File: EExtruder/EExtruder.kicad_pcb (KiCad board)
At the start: 2 copper layers, 66.2 x 47.1 mm, 86 parts, among them J1 20A 50V, J11 Conn_01x03_Male, J2 AudioJack4_Ground, J3 6A 50V, J4 6A 50V, J5 Conn_01x02, J6 Conn_01x02, J7 Conn_01x03_Male, J8 Conn_01x03_Male, J9 Conn_01x03_Male, Q1 DTC124E, Q2 PSMN7R0-30YL, Q3 DTC124E, Q4 PSMN7R0-30YL, Q5 SI2318CDS, Q6 SI2318CDS, Q7 SI2318CDS, U1 STM32F030C8Tx, U2 DCBuck, Y1 8MHz

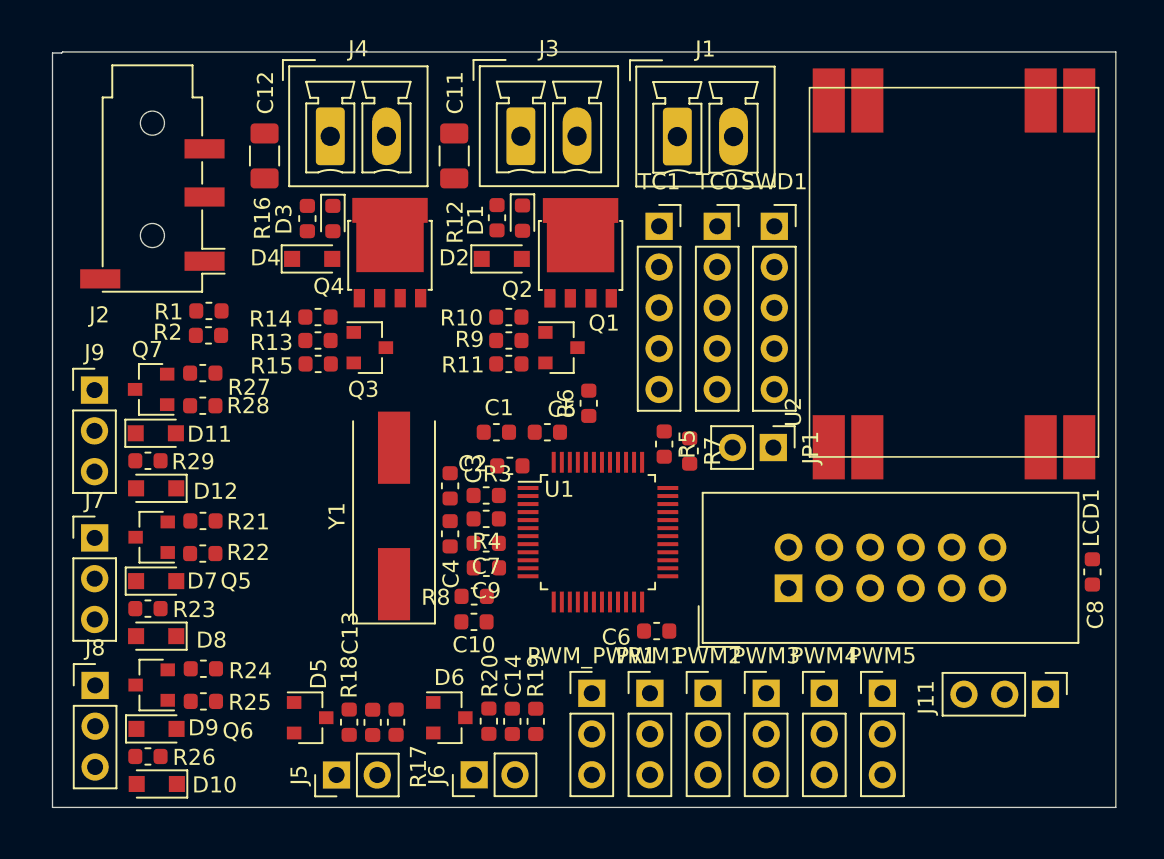
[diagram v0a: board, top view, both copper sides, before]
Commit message: 32 traces to go.
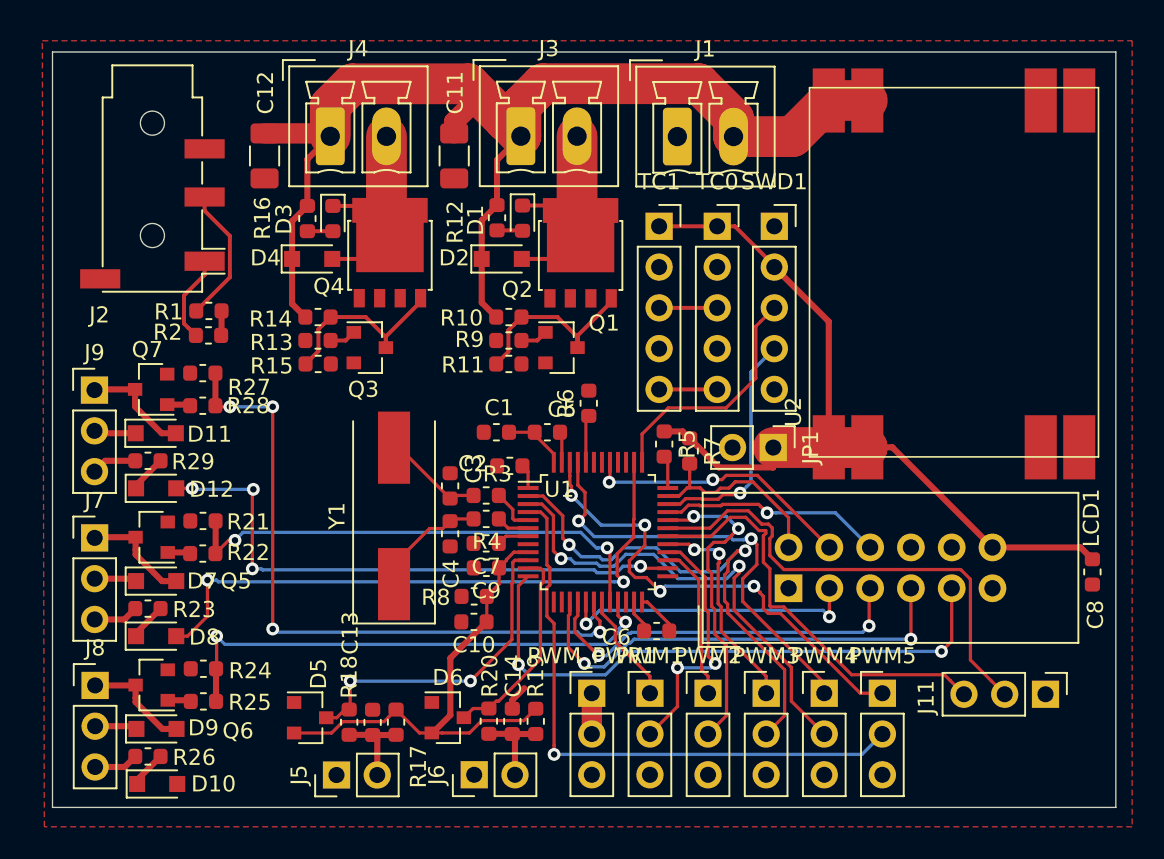
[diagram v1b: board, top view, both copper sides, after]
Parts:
- moved D6 0.10 mm to (152.6, 124.6)
- turned D10 to 0 degrees
- turned D12 to 0 degrees
- turned D8 to 0 degrees
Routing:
- net /VIN: track 0.00 -> 86.0 mm
- net /3.3V: track 0.00 -> 62.4 mm
- net /PWM0: track 0.00 -> 42.1 mm, vias 0 -> 4
- net /TACH_E0: track 0.00 -> 38.7 mm, vias 0 -> 2
- net /TACH5: track 0.00 -> 37.3 mm, vias 0 -> 1
- net /TEMP_EX: track 0.00 -> 37.2 mm, vias 0 -> 2
- net /TACH0: track 0.00 -> 36.0 mm, vias 0 -> 4
- net /SPI_CLK: track 0.00 -> 32.2 mm, vias 0 -> 2
- net /E1_FAN: track 0.00 -> 31.9 mm, vias 0 -> 2
- net /TACH3: track 0.00 -> 31.8 mm, vias 0 -> 2
- net /AVREF: track 0.00 -> 31.2 mm
- net /E0_FAN: track 0.00 -> 30.8 mm, vias 0 -> 2
- net /PWM5: track 0.00 -> 30.4 mm, vias 0 -> 4
- net /UART_RX: track 0.00 -> 30.3 mm
- net /TACH4: track 0.00 -> 30.2 mm, vias 0 -> 2
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- added copper zone on F.Cu, net GND
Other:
- outline, holes or cut-outs redrawn

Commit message: Unrouted - only power.
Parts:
- moved JP1 28.8 mm to (144.1, 106.6), turned to 0 degrees
- moved C10 6.51 mm to (148.6, 122.0)
- moved C9 5.82 mm to (156.5, 120.9), turned to 90 degrees
- moved R8 5.48 mm to (158.1, 120.9), turned to 90 degrees
- moved R7 5.00 mm to (172.6, 108.6)
- moved R5 4.95 mm to (170.9, 108.6)
- moved C7 1.07 mm to (154.2, 114.5), turned to 270 degrees
- moved R6 0.96 mm to (162.3, 104.7), turned to 0 degrees
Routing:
- net /3.3V: track 62.4 -> 9.73 mm
- net /PWM0: track 42.1 -> 2.03 mm, vias 4 -> 0
- net /TACH_E0: track 38.7 -> 0.00 mm, vias 2 -> 0
- net /TACH5: track 37.3 -> 0.00 mm, vias 1 -> 0
- net /TEMP_EX: track 37.2 -> 0.00 mm, vias 2 -> 0
- net /TACH0: track 36.0 -> 0.00 mm, vias 4 -> 0
- net /SPI_CLK: track 32.2 -> 0.00 mm, vias 2 -> 0
- net /TACH3: track 31.8 -> 0.00 mm, vias 2 -> 0
- net /AVREF: track 31.2 -> 0.00 mm
- net /PWM5: track 30.4 -> 0.00 mm, vias 4 -> 0
- net /UART_RX: track 30.3 -> 0.00 mm
- net /TACH4: track 30.2 -> 0.00 mm, vias 2 -> 0
- net /E1_FAN: track 31.9 -> 2.03 mm, vias 2 -> 0
- net /E0_FAN: track 30.8 -> 2.04 mm, vias 2 -> 0
- net /MISO: track 27.6 -> 0.00 mm, vias 2 -> 0
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
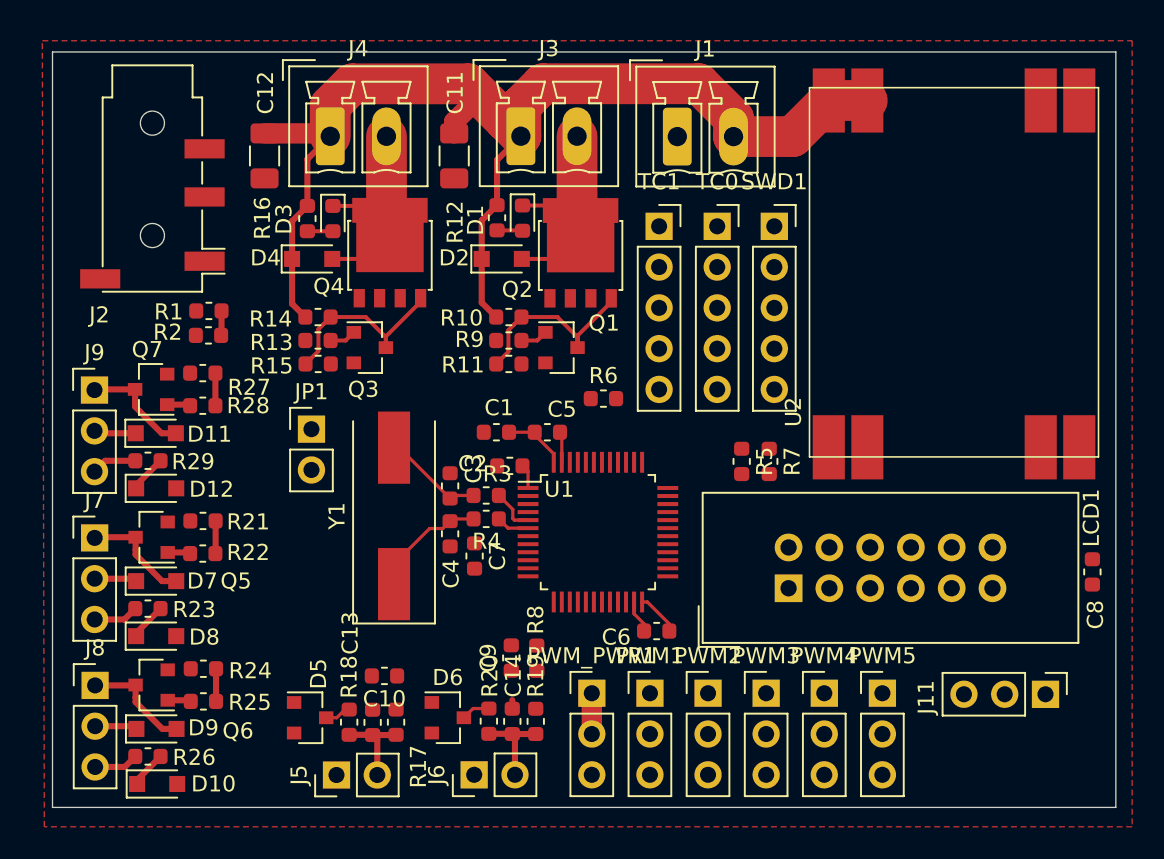
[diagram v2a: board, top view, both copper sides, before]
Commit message: All routed - thank you autorouter.
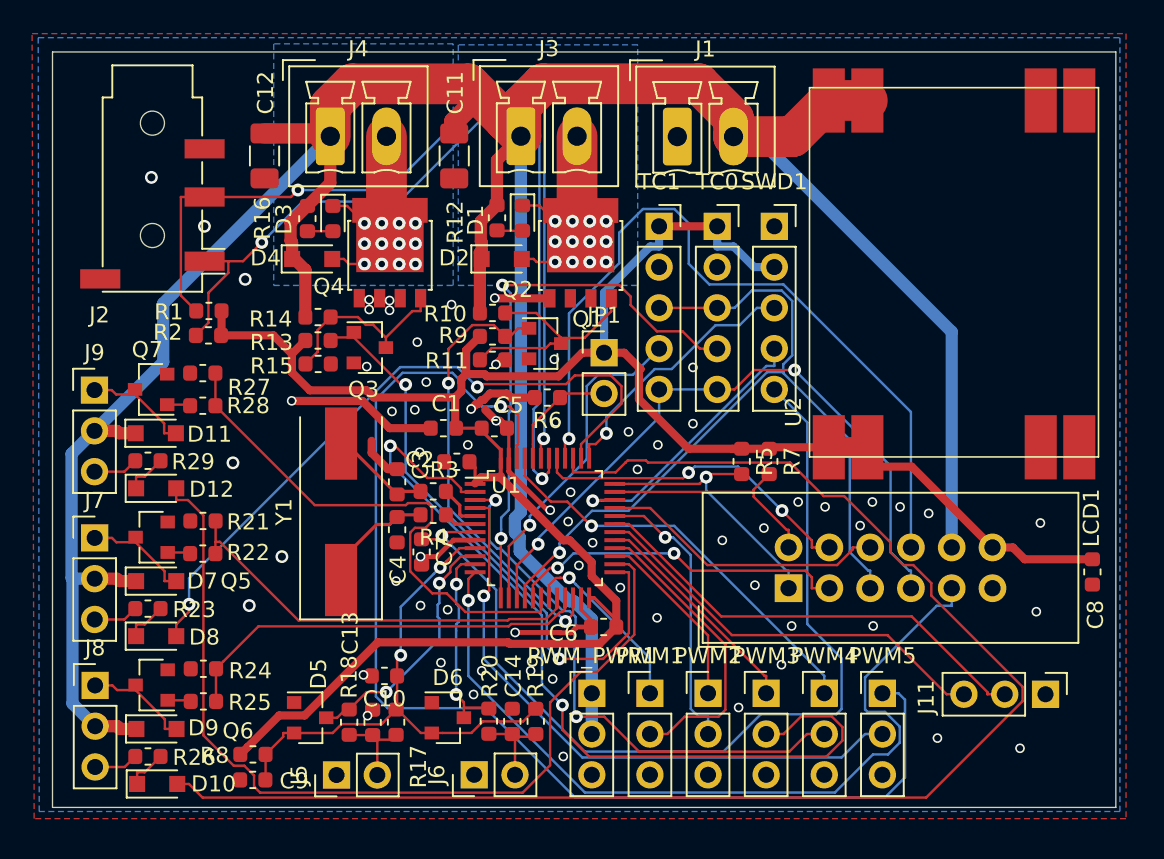
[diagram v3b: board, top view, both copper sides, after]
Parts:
- moved JP1 18.8 mm to (162.3, 101.9)
- moved R8 18.7 mm to (140.4, 126.9), turned to 180 degrees
- moved C9 17.8 mm to (140.4, 128.5), turned to 180 degrees
- moved R6 3.49 mm to (158.8, 104.6), turned to 180 degrees
- moved C2 3.31 mm to (153.1, 108.6)
- moved C1 3.31 mm to (152.3, 106.6)
- moved C6 3.31 mm to (162.3, 118.9)
- moved Y1 3.31 mm to (145.9, 111.8)
- moved U1 3.31 mm to (158.6, 112.8)
- moved R4 3.31 mm to (151.7, 112.0)
- moved C3 3.31 mm to (149.4, 109.9)
- moved C5 3.31 mm to (155.5, 106.6)
- moved C7 3.31 mm to (150.9, 114.3)
- moved R3 3.31 mm to (151.7, 110.5)
- moved C4 3.31 mm to (149.4, 112.9)
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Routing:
- net /3.3V: track 9.73 -> 142.1 mm
- net /VIN: track 86.0 -> 200.7 mm
- net /TACH_E1: track 0.00 -> 92.2 mm
- net /PWM5: track 0.00 -> 74.5 mm, vias 0 -> 1
- net /~RESET: track 0.00 -> 59.4 mm, vias 0 -> 1
- net /TACH0: track 0.00 -> 57.0 mm
- net /SCL: track 0.00 -> 55.4 mm, vias 0 -> 2
- net /SDA: track 0.00 -> 54.9 mm, vias 0 -> 2
- net /TACH3: track 0.00 -> 53.6 mm, vias 0 -> 2
- net /MISO: track 0.00 -> 52.2 mm, vias 0 -> 1
- net /TEMP_EX: track 0.00 -> 51.7 mm, vias 0 -> 1
- net /EXT2: track 0.00 -> 49.4 mm, vias 0 -> 1
- net /TACH_E0: track 0.00 -> 42.9 mm, vias 0 -> 2
- net /SPI_CLK: track 0.00 -> 42.3 mm, vias 0 -> 2
- net /TACH5: track 0.00 -> 38.4 mm, vias 0 -> 1
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- added copper zone on B.Cu, net GND
- added copper zone on B.Cu, net Net-(D1-Pad1)
- added copper zone on B.Cu, net Net-(D3-Pad1)
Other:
- net class Default: clearance 0.2 -> 0.1524; trace_width 0.25 -> 0.1524
- net class V24 added: clearance 0.1524, trace_width 0.762, via_dia 0.8, via_drill 0.4
- net class V33 added: clearance 0.1524, trace_width 0.508, via_dia 0.8, via_drill 0.4
- rule trace_clearance: 0.2 -> 0.1524
- rule trace_min: 0.2 -> 0.127
- rule via_min_size: 0.4 -> 0.6

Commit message: Ready to manufacture.
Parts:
- added H1: MountingHole, MountingHole:MountingHole_3.2mm_M3, F.Cu at (142.4, 122.0)
- added H2: MountingHole, MountingHole:MountingHole_3.2mm_M3, F.Cu at (188.8, 126.7)
- moved C8 9.62 mm to (185.1, 109.6), turned to 0 degrees
- moved J11 8.14 mm to (183.4, 128.1), turned to 180 degrees
- moved D5 3.35 mm to (142.1, 127.3)
- moved R8 1.71 mm to (138.8, 126.4)
- moved C9 1.68 mm to (138.8, 128.1)
- moved C13 0.06 mm to (147.9, 124.8)
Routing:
- net GND: track 40.6 -> 47.6 mm, vias 67 -> 131
- net /TEMP0: track 15.8 -> 18.8 mm
- net /TACH0: track 57.0 -> 59.8 mm
- net /AVREF: track 33.6 -> 36.2 mm
- net /TACH_E1: track 92.2 -> 90.3 mm
- net /UART_TX: track 25.9 -> 24.6 mm
- net /3.3V: track 142.1 -> 140.9 mm
- net /UART_RX: track 28.8 -> 29.9 mm
- net /TEMP_EX: track 51.7 -> 51.2 mm
- net /SDA2: track 17.3 -> 17.8 mm
- added copper zone on F.Cu, net Net-(D1-Pad1)
- added copper zone on F.Cu, net Net-(D3-Pad1)
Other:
- board size 66.2 x 47.1 mm -> 64.4 x 47.1 mm
- board text added: "+ -"
- board text added: "- +"
- board text added: "3.3v"
- board text added: "BOOT"
- board text added: "COOL"
- board text added: "EXT1"
- board text added: "EXT2"
- board text added: "FAN0"
- board text added: "FAN1"
- board text added: "GND"
- board text added: "HEAT0"
- board text added: "HEAT1"
- board text added: "LED"
- board text added: "MISO"
- board text added: "MOSI"
- board text added: "SCK"
- board text added: "SCL"
- board text added: "SDA"
- board text added: "T + -"
- board text added: "T0"
- board text added: "T1"
- board text added: "TC0"
- board text added: "TC1"
- board text added: "TMP EX"
- board text added: "Vin"
- board text added: "swclk"
- board text added: "swdio"
- board text added: "~reset"

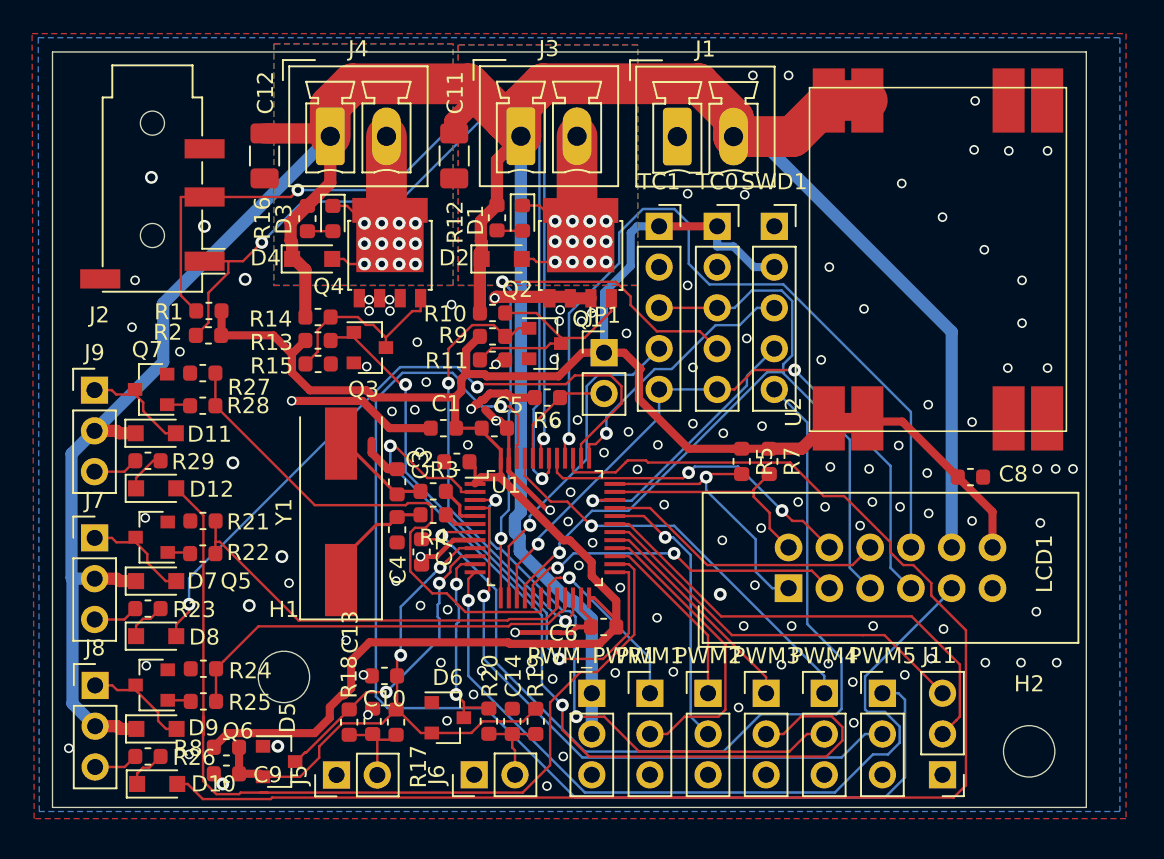
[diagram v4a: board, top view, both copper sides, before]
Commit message: Select correct terminals. Use old style square footprints.
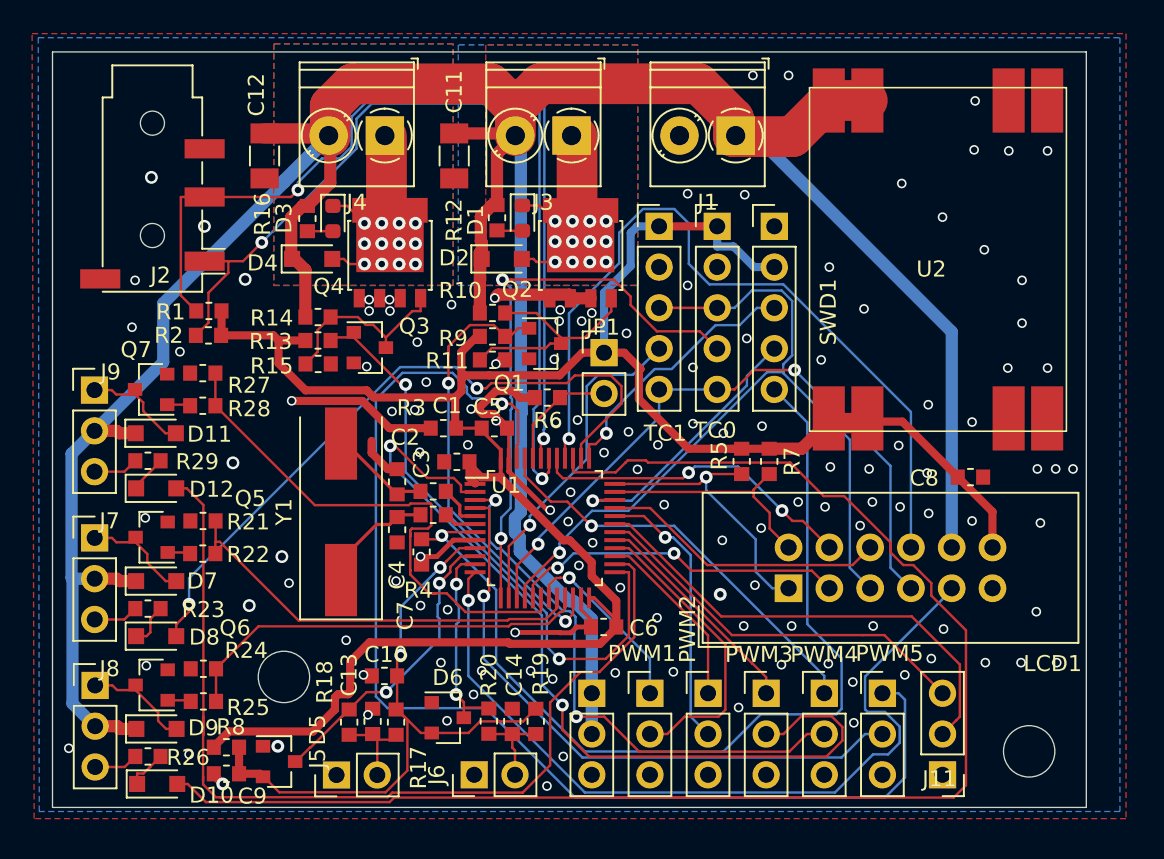
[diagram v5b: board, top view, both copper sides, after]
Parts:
- C1, C10, C13, C14, C2, C3, C4, C5, C6, C7, C8, C9: footprint Capacitor_SMD:C_0603_1608Metric -> Local:C_0603_1608Metric
- C11, C12: footprint Capacitor_SMD:C_1206_3216Metric -> Local:C_1206_3216Metric
- J1, J3, J4: footprint Connector_Phoenix_MC:PhoenixContact_MCV_1,5_2-G-3.5_1x02_P3.50mm_Vertical -> Local:TerminalBlock_Phoenix_PT-1,5-2-3.5-H_1x02_P3.50mm_Horizontal
- R1, R10, R11, R12, R13, R14, R15, R16, R17, R18, R19, R2, R20, R21, R22, R23, R24, R25, R26, R27, R28, R29, R3, R4, R5, R6, R7, R8, R9: footprint Resistor_SMD:R_0603_1608Metric -> Local:R_0603_1608Metric
- SWD1, TC0, TC1: footprint Connector_PinSocket_2.54mm:PinSocket_1x05_P2.54mm_Vertical -> Connector_PinHeader_2.54mm:PinHeader_1x05_P2.54mm_Vertical
- moved J1 3.64 mm to (170.5, 88.3), turned to 180 degrees
- moved J4 3.40 mm to (148.7, 88.3), turned to 180 degrees
- moved J3 3.16 mm to (160.3, 88.3), turned to 180 degrees
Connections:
- J1 pad 1: GND -> /VIN
- J1 pad 2: /VIN -> GND
- J3 pad 1: /VIN -> Net-(D1-Pad1)
- J3 pad 2: Net-(D1-Pad1) -> /VIN
- J4 pad 1: /VIN -> Net-(D3-Pad1)
- J4 pad 2: Net-(D3-Pad1) -> /VIN
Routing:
- net /VIN: track 200.7 -> 204.9 mm
- net /AVREF: track 36.2 -> 39.9 mm
- net GND: track 47.6 -> 45.0 mm
- net /3.3V: track 140.9 -> 143.4 mm
- net /SDA: track 54.9 -> 56.3 mm
- net /SCL: track 55.4 -> 56.5 mm
- net /PWM0: track 33.2 -> 34.1 mm
- net /TEMP0: track 18.8 -> 19.5 mm
